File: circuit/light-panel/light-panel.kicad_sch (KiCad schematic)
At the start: 30 parts, among them J1 Screw_Terminal_01x02

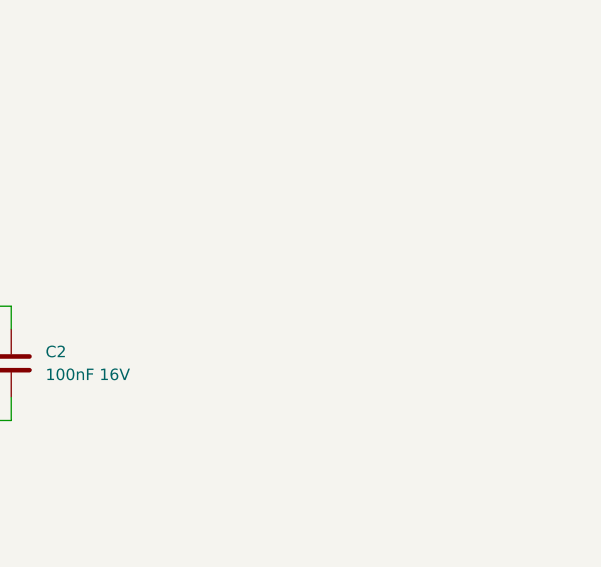
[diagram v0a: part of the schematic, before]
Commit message: Add holding screw
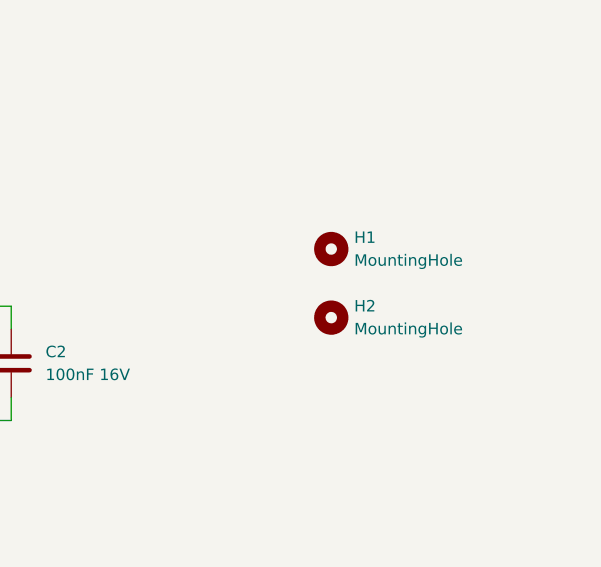
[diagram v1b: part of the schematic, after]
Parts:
- added H1, H2: MountingHole, MountingHole:MountingHole_2.2mm_M2, symbol Mechanical:MountingHole
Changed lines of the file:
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@@
+	)
+	(symbol
+		(lib_id "Mechanical:MountingHole")
+		(at 158.75 151.13 0)
+		(unit 1)
+		(body_style 1)
+		(exclude_from_sim no)
+		(in_bom no)
+		(on_board yes)
+		(in_pos_files yes)
+		(dnp no)
+		(fields_autoplaced yes)
+		(property "Reference" "H1"
+			(at 161.29 149.8599 0)
+			(show_name no)
+			(do_not_autoplace no)
+			(effects
+				(font
+					(size 1.27 1.27)
+				)
+				(justify left)
+			)
+		)
+		(property "Value" "MountingHole"
+			(at 161.29 152.3999 0)
+			(show_name no)
+			(do_not_autoplace no)
+			(effects
+				(font
+					(size 1.27 1.27)
+				)
+				(justify left)
+			)
+		)
+		(property "Footprint" "MountingHole:MountingHole_2.2mm_M2"
+			(at 158.75 151.13 0)
+			(hide yes)
+			(show_name no)
+			(do_not_autoplace no)
+			(effects
+				(font
+					(size 1.27 1.27)
+				)
+			)
+		)
+		(property "Datasheet" ""
+			(at 158.75 151.13 0)
+			(hide yes)
+			(show_name no)
+			(do_not_autoplace no)
+			(effects
+				(font
+					(size 1.27 1.27)
+				)
+			)
+		)
+		(property "Description" "Mounting Hole without connection"
+			(at 158.75 151.13 0)
+			(hide yes)
+			(show_name no)
+			(do_not_autoplace no)
+			(effects
+				(font
+					(size 1.27 1.27)
+				)
+			)
+		)
+		(instances
+			(project "light-panel"
+				(path "/0e30cdad-82ec-4068-ae59-974c84c5b947"
+					(reference "H1")
+					(unit 1)
+				)
+			)
+		)
 	)
 	(symbol
@@
 					(unit 1)
 				)
+			)
+		)
+	)
+	(symbol
+		(lib_id "Mechanical:MountingHole")
+		(at 158.75 158.75 0)
+		(unit 1)
+		(body_style 1)
+		(exclude_from_sim no)
+		(in_bom no)
+		(on_board yes)
+		(in_pos_files yes)
+		(dnp no)
+		(fields_autoplaced yes)
+		(property "Reference" "H2"
+			(at 161.29 157.4799 0)
+			(show_name no)
+			(do_not_autoplace no)
+			(effects
+				(font
+					(size 1.27 1.27)
+				)
+				(justify left)
+			)
+		)
+		(property "Value" "MountingHole"
+			(at 161.29 160.0199 0)
+			(show_name no)
+			(do_not_autoplace no)
+			(effects
+				(font
+					(size 1.27 1.27)
+				)
+				(justify left)
+			)
+		)
+		(property "Footprint" "MountingHole:MountingHole_2.2mm_M2"
+			(at 158.75 158.75 0)
+			(hide yes)
+			(show_name no)
+			(do_not_autoplace no)
+			(effects
+				(font
+					(size 1.27 1.27)
+				)
+			)
+		)
+		(property "Datasheet" ""
+			(at 158.75 158.75 0)
+			(hide yes)
+			(show_name no)
+			(do_not_autoplace no)
+			(effects
+				(font
+					(size 1.27 1.27)
+				)
+			)
+		)
+		(property "Description" "Mounting Hole without connection"
+			(at 158.75 158.75 0)
+			(hide yes)
+			(show_name no)
+			(do_not_autoplace no)
+			(effects
+				(font
+					(size 1.27 1.27)
+				)
+			)
+		)
+		(instances
+			(project "light-panel"
+				(path "/0e30cdad-82ec-4068-ae59-974c84c5b947"
+					(reference "H2")
+					(unit 1)
+				)
